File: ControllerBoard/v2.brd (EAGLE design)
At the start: 121.5 x 69 mm, 28 parts, among them J5 U-F-M5DD-Y-L, SW1 SPST_TACT-EVQQ2, SW2 SPST_TACT-EVQQ2, SW6 SPST_TACT-EVQQ2, U1 JOYSTICKPTH, U3 JOYSTICKPTH, U4 SPX3819-3.3, U5 MCP73831T-2ACI/OT, X1 JSTPH

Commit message: Do the thing
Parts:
- removed SW1, SW2, SW6: SPST_TACT-EVQQ2, adafruit:EVQ-Q2
- added R10, R11, R12: 10k, adafruit:R0603
- added U$1: RPI-ZERO, RPI-Zero:RASPBERRYPI_BASTELSTUBE_V13_RASPI_BOARD_B+_FULL
- added U$10, U$12, U$13, U$14, U$8, U$9: CHERRY-MX-LED, cherrymx:CHERRY-MX-LED
- added U2: MCP3008-I/SL, MCP3008-I_SL:SOIC127P600X175-16N
- moved C8 86.6 mm to (94.0, 88.9), flipped to the top, turned to 0 degrees
- moved J5 79.3 mm to (44.5, 64.8), flipped to the top, turned to 0 degrees
- moved C5 78.6 mm to (100.3, 88.9), flipped to the top
- moved R4 74.7 mm to (71.1, 88.9), flipped to the top
- moved R3 73.8 mm to (76.2, 88.9), flipped to the top
- moved R7 70.5 mm to (66.0, 88.9), flipped to the top
- moved C9 69.6 mm to (87.6, 88.9), flipped to the top
- moved C13 69.5 mm to (106.7, 88.9), flipped to the top, turned to 0 degrees
- moved C14 67.9 mm to (81.3, 88.9), flipped to the top
- moved R1 65.2 mm to (90.2, 80.0), flipped to the top
- moved X1 64.6 mm to (26.7, 69.8), flipped to the top
- moved C7 62.5 mm to (50.8, 88.9), flipped to the top, turned to 0 degrees
- moved R8 61.1 mm to (61.0, 88.9), flipped to the top
- moved D1 60.0 mm to (71.1, 78.7), flipped to the top, turned to 0 degrees
- moved R9 59.8 mm to (55.9, 88.9), flipped to the top, turned to 0 degrees
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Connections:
- new net BTN_D: R10.1, U$12.SW1
- new net BTN_E: R11.1, U$13.SW1
- new net BTN_F: R12.1, U$14.SW1
- new net CE0: U$1.24, U2.10
- new net MISO: U$1.21, U2.12
- new net MOSI: U$1.19, U2.11
- new net SCLK: U$1.23, U2.13
- net 3.3V: now also R10.2, R11.2, R12.2, U2.15, U2.16
- net BTN_A: now also U$1.29, U$8.SW1; no longer SW6.B, SW6.B'
- net BTN_B: now also U$1.31, U$9.SW1; no longer SW1.B, SW1.B'
- net BTN_C: now also U$1.33, U$10.SW1; no longer SW2.B, SW2.B'
- net GND: now also U$10.SW2, U$12.SW2, U$13.SW2, U$14.SW2, U$8.SW2, U$9.SW2, U2.14, U2.9; no longer SW1.A, SW1.A', SW2.A, SW2.A', SW6.A, SW6.A'
- net H1: now also U2.2
- net H2: now also U2.4
- net V1: now also U2.1
- net V2: now also U2.3
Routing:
- removed copper zone on layer 1, net GND
- removed copper zone on layer 16, net GND
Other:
- board size 121.5 x 69 mm -> 160 x 100 mm
- board text removed: "BUILDING BLOCK STUDIO"
- board text removed: "Button A"
- board text removed: "Button B"
- board text removed: "Extra"
- board text removed: "Reset"
- board text removed: "Robot Controller"
- board text removed: "V0.9"

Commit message: Boards ready for review
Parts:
- removed U$10, U$12, U$13, U$14, U$8, U$9: CHERRY-MX-LED, cherrymx:CHERRY-MX-LED
- removed X1: JSTPH, microbuilder:JSTPH2
- added CN1: (no value), adafruit:JST-PH-2-THM-RA
- added S1, S2, S3, S4, S5, S6: B3F-4050, B3F-4050:SW_B3F-4050
- moved R10 186.9 mm to (102.0, 79.9), flipped to the bottom
- moved R12 185.9 mm to (102.0, 82.0), flipped to the bottom
- moved R11 185.1 mm to (102.0, 84.0), flipped to the bottom
- moved SW4 90.2 mm to (92.1, 60.7), flipped to the bottom, turned to 0 degrees
- moved U1 62.0 mm to (145.0, 84.4)
- moved U3 61.1 mm to (15.1, 84.4)
- moved J5 56.8 mm to (101.1, 60.2), flipped to the bottom
- moved CHG 45.9 mm to (107.9, 59.8), flipped to the bottom, turned to 90 degrees
- moved R3 41.3 mm to (107.9, 62.4), flipped to the bottom
- moved R8 39.4 mm to (98.9, 78.2), flipped to the bottom, turned to 180 degrees
- moved U$1 38.5 mm to (54.8, 89.3)
- moved ON4 31.0 mm to (85.5, 59.8), flipped to the bottom, turned to 90 degrees
- moved U2 28.1 mm to (89.0, 81.0), flipped to the bottom, turned to 270 degrees
- moved C13 27.6 mm to (79.6, 83.3), flipped to the bottom, turned to 180 degrees
- moved C5 23.3 mm to (79.6, 78.3), flipped to the bottom, turned to 180 degrees
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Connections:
- new net N$7: U$1.40
- net BATTERY_SENSE: now also U2.5
- net BTN_A: now also S1.3, S1.4; no longer U$8.SW1
- net BTN_B: now also S5.3, S5.4; no longer U$9.SW1
- net BTN_C: now also S6.3, S6.4; no longer U$10.SW1
- net BTN_D: now also S2.3, S2.4, U$1.35; no longer U$12.SW1
- net BTN_E: now also S3.3, S3.4, U$1.37; no longer U$13.SW1
- net BTN_F: now also S4.3, S4.4, U$1.38; no longer U$14.SW1
- net GND: now also CN1.2, S1.1, S1.2, S2.1, S2.2, S3.1, S3.2, S4.1, S4.2, S5.1, S5.2, S6.1, S6.2; no longer U$10.SW2, U$12.SW2, U$13.SW2, U$14.SW2, U$8.SW2, U$9.SW2, X1.1
- net N$2: now also CN1.1; no longer X1.2
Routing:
- net 3.3V: track 0.00 -> 269.4 mm
- net BTN_A: track 0.00 -> 170.3 mm, vias 0 -> 5
- net V1: track 0.00 -> 99.9 mm, vias 0 -> 4
- net H2: track 0.00 -> 98.2 mm, vias 0 -> 4
- net BTN_C: track 0.00 -> 92.8 mm, vias 0 -> 5
- net BTN_B: track 0.00 -> 90.7 mm, vias 0 -> 7
- net VBUS: track 0.00 -> 83.6 mm, vias 0 -> 4
- net H1: track 0.00 -> 81.2 mm, vias 0 -> 4
- net BATTERY_SENSE: track 0.00 -> 72.1 mm, vias 0 -> 4
- net BTN_F: track 0.00 -> 68.2 mm, vias 0 -> 2
- net N$3: track 0.00 -> 64.0 mm, vias 0 -> 6
- net V2: track 0.00 -> 63.0 mm, vias 0 -> 4
- net BTN_E: track 0.00 -> 55.6 mm
- net N$4: track 0.00 -> 45.7 mm, vias 0 -> 6
- net CE0: track 0.00 -> 37.5 mm, vias 0 -> 2
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- added copper zone on layer 1, net GND
- added copper zone on layer 16, net GND
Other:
- board size 160 x 100 mm -> 163 x 59 mm
- board text added: "+"
- board text added: "-"
- board text added: "C:/Users/CodyS/OneDrive - Queensland University of Technology/Uni Coursework/2021/EGH419 Group 1 Shared Folder/Git Stuff/EGH419/LOGO.bmp"

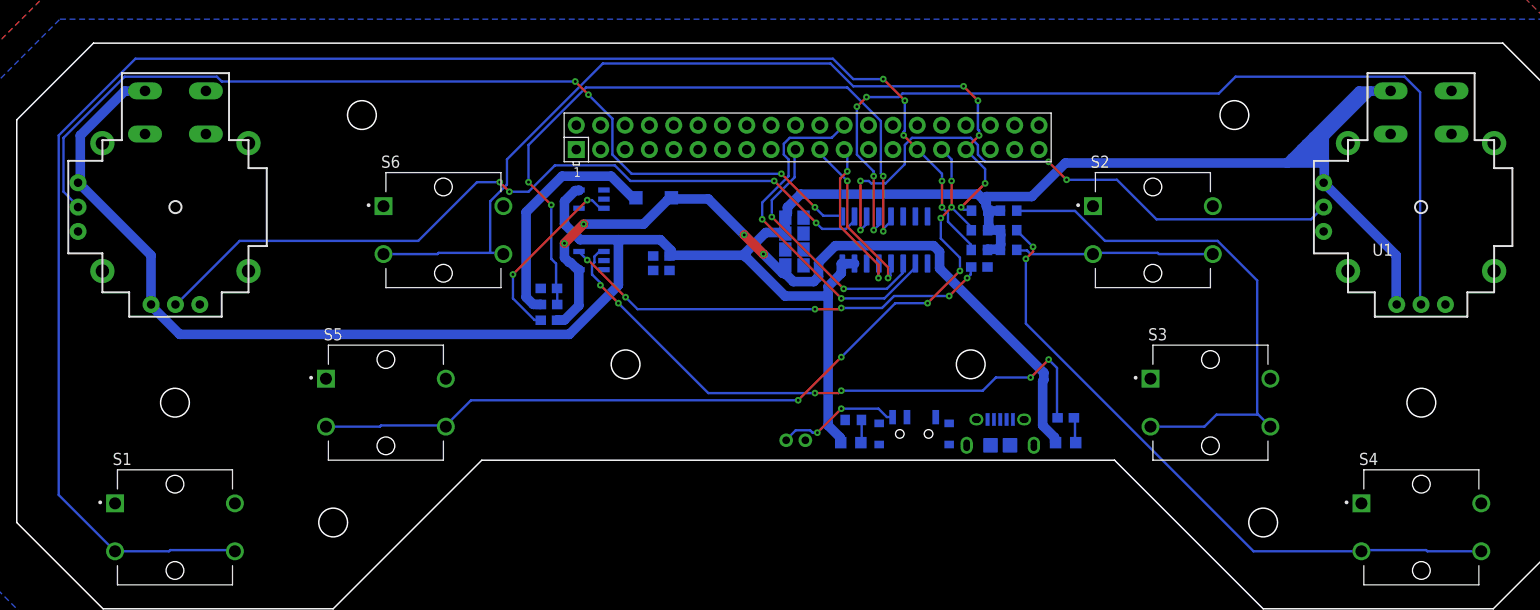
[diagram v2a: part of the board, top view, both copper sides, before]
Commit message: Added Breakout Board2
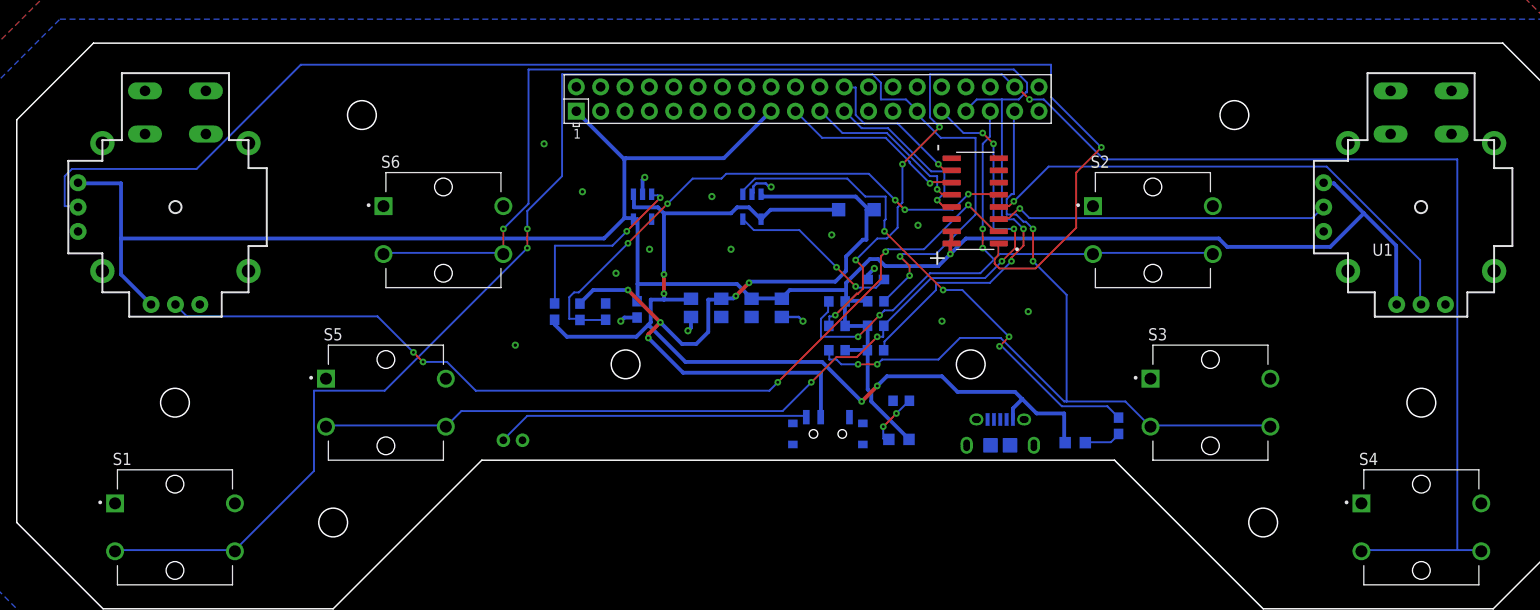
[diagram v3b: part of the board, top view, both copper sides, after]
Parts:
- removed C14: 1uF, microbuilder:0603-NO
- moved CN1 29.5 mm to (50.2, 60.1)
- moved R11 23.1 mm to (84.0, 69.5), turned to 180 degrees
- moved D1 21.2 mm to (86.1, 84.1), turned to 180 degrees
- moved R12 20.5 mm to (84.0, 72.0), turned to 180 degrees
- moved R10 18.7 mm to (84.0, 74.6), turned to 180 degrees
- moved R2 18.2 mm to (88.1, 69.5), turned to 0 degrees
- moved U5 17.7 mm to (75.2, 84.4), turned to 180 degrees
- moved R1 14.7 mm to (88.1, 72.0), turned to 0 degrees
- moved R6 12.1 mm to (88.1, 74.6), turned to 0 degrees
- moved C5 11.7 mm to (68.8, 73.9), turned to 270 degrees
- moved R8 10.9 mm to (88.1, 76.8), turned to 0 degrees
- moved U2 10.3 mm to (98.5, 85.0), flipped to the top, turned to 180 degrees
- moved C9 9.76 mm to (72.0, 73.9), turned to 270 degrees
- moved C13 9.50 mm to (78.3, 73.9), turned to 270 degrees
- moved SW4 9.00 mm to (83.1, 60.7)
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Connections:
- removed net AREF: C14.1
- removed net B_1: U3.B2A
- removed net B_2: U1.B2A
- net 3.3V: now also U$1.1, U$1.17; no longer U1.B1A, U3.B1A
- net GND: now also U$1.14, U$1.20, U$1.25, U$1.30, U$1.34, U$1.39, U$1.6, U$1.9; no longer C14.2
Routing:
- net BTN_F: track 68.2 -> 145.0 mm, vias 2 -> 5
- net VBAT: track 24.7 -> 82.3 mm, vias 0 -> 5
- net V1: track 99.9 -> 145.3 mm, vias 4 -> 1
- net BTN_D: track 20.7 -> 64.9 mm, vias 0 -> 4
- net H2: track 98.2 -> 54.5 mm, vias 4 -> 1
- net BTN_C: track 92.8 -> 130.7 mm, vias 5 -> 3
- net 3.3V: track 269.4 -> 237.8 mm, vias 0 -> 1
- net BTN_E: track 55.6 -> 86.4 mm, vias 0 -> 4
- net V2: track 63.0 -> 35.2 mm, vias 4 -> 1
- net N$4: track 45.7 -> 18.0 mm, vias 6 -> 2
- net VBUS: track 83.6 -> 106.5 mm
- net CE0: track 37.5 -> 16.5 mm, vias 2 -> 1
- net N$2: track 13.1 -> 32.7 mm, vias 2 -> 0
- net H1: track 81.2 -> 100.2 mm, vias 4 -> 5
- net BTN_A: track 170.3 -> 151.8 mm, vias 5 -> 4
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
